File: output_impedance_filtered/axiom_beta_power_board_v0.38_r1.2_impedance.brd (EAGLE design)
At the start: 101.6 x 57.1 mm, 0 parts

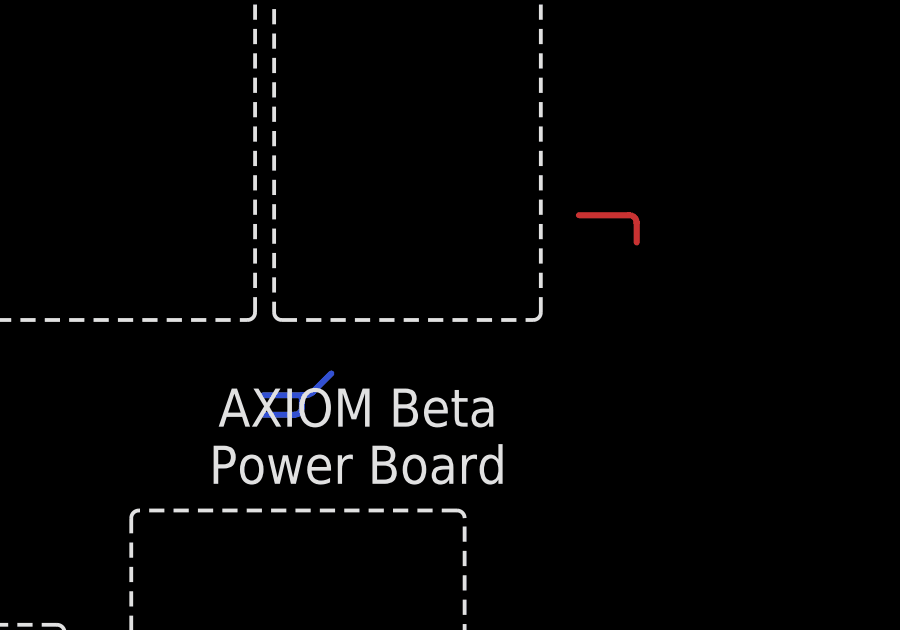
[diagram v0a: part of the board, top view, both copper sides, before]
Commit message: updated impedance filtered output brds
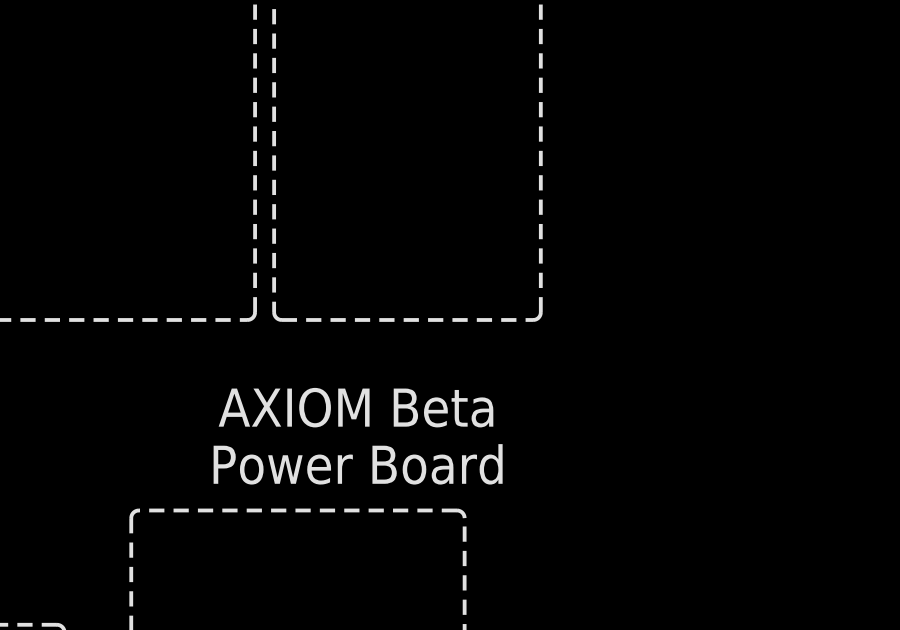
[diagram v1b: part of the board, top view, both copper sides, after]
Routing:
- net A_BUS_EN: track 18.6 -> 0.00 mm
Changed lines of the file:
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@@
 <setting verticaltext="up"/>
 </settings>
-<grid distance="25" unitdist="mil" unit="mil" style="lines" multiple="1" display="yes" altdistance="12.5" altunitdist="mil" altunit="mil"/>
+<grid distance="0.05" unitdist="inch" unit="inch" style="lines" multiple="1" display="yes" altdistance="0.025" altunitdist="inch" altunit="inch"/>
 <layers>
 <layer number="1" name="Top" color="16" fill="1" visible="yes" active="yes"/>
@@
 <layer number="25" name="tNames" color="7" fill="1" visible="yes" active="yes"/>
 <layer number="26" name="bNames" color="7" fill="1" visible="yes" active="yes"/>
-<layer number="27" name="tValues" color="11" fill="1" visible="yes" active="yes"/>
-<layer number="28" name="bValues" color="11" fill="1" visible="yes" active="yes"/>
+<layer number="27" name="tValues" color="11" fill="1" visible="no" active="yes"/>
+<layer number="28" name="bValues" color="11" fill="1" visible="no" active="yes"/>
 <layer number="29" name="tStop" color="7" fill="3" visible="yes" active="yes"/>
 <layer number="30" name="bStop" color="7" fill="6" visible="yes" active="yes"/>
@@
 <signal name="NC$2" class="1">
 </signal>
-<signal name="A_BUS_EN" class="1">
-<wire x1="29.865" y1="7.665" x2="29.865" y2="8.3185" width="0.2032" layer="1"/>
-<wire x1="29.865" y1="8.3185" x2="29.611" y2="8.5725" width="0.2032" layer="1" curve="90"/>
-<wire x1="29.611" y1="8.5725" x2="27.94" y2="8.5725" width="0.2032" layer="1"/>
-<wire x1="26.8605" y1="6.190315625" x2="26.8605" y2="8.1915" width="0.2032" layer="2"/>
-<wire x1="26.8605" y1="8.1915" x2="27.2415" y2="8.5725" width="0.2032" layer="2" curve="-90"/>
-<wire x1="27.2415" y1="8.5725" x2="27.94" y2="8.5725" width="0.2032" layer="2"/>
-<wire x1="26.8605" y1="6.190315625" x2="26.74890625" y2="5.92090625" width="0.2032" layer="2" curve="-45.000332"/>
-<wire x1="26.74890625" y1="5.92090625" x2="25.57509375" y2="4.74709375" width="0.2032" layer="2"/>
-<wire x1="25.57509375" y1="4.74709375" x2="25.305684375" y2="4.6355" width="0.2032" layer="2" curve="-45.00047"/>
-<wire x1="25.305684375" y1="4.6355" x2="21.183315625" y2="4.6355" width="0.2032" layer="2"/>
-<wire x1="21.183315625" y1="4.6355" x2="20.91390625" y2="4.52390625" width="0.2032" layer="2" curve="45.000332"/>
-<wire x1="20.91390625" y1="4.52390625" x2="19.685" y2="3.295" width="0.2032" layer="2"/>
-<wire x1="18.706" y1="2.57" x2="18.706" y2="2.174" width="0.2032" layer="16"/>
-<wire x1="18.706" y1="2.174" x2="18.452" y2="1.92" width="0.2032" layer="16" curve="-90"/>
-<wire x1="18.452" y1="1.92" x2="17.42" y2="1.92" width="0.2032" layer="16"/>
-<wire x1="17.42" y1="2.57" x2="18.706" y2="2.57" width="0.2032" layer="16"/>
-<wire x1="19.685" y1="3.295" x2="19.07159375" y2="2.68159375" width="0.2032" layer="16"/>
-<wire x1="19.07159375" y1="2.68159375" x2="18.802184375" y2="2.57" width="0.2032" layer="16" curve="-45.00047"/>
-<wire x1="18.802184375" y1="2.57" x2="18.706" y2="2.57" width="0.2032" layer="16"/>
-</signal>
 </signals>
